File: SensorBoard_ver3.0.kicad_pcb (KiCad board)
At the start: 2 copper layers, 75 x 50 mm, 58 parts, among them IC1 MIC5504-3.3YM5-T5, J1 STLink, J10 Abs1, J11 Abs3, J12 Limit1, J13 Limit2, J14 Abs3, J2 Enc0, J3 Enc2, J4 CANConn, J5 Enc1, J6 Enc3, J7 CANConn, J8 Abs0, J9 Abs2, SW1 CAN_Terminal, SW2 IDSetSW, SW3 Reset, SW4 IDSetSW, U1 L7805, U2 MAX3485, U3 ATA6561, U4 STM32F303K8Tx, Y1 Crystal

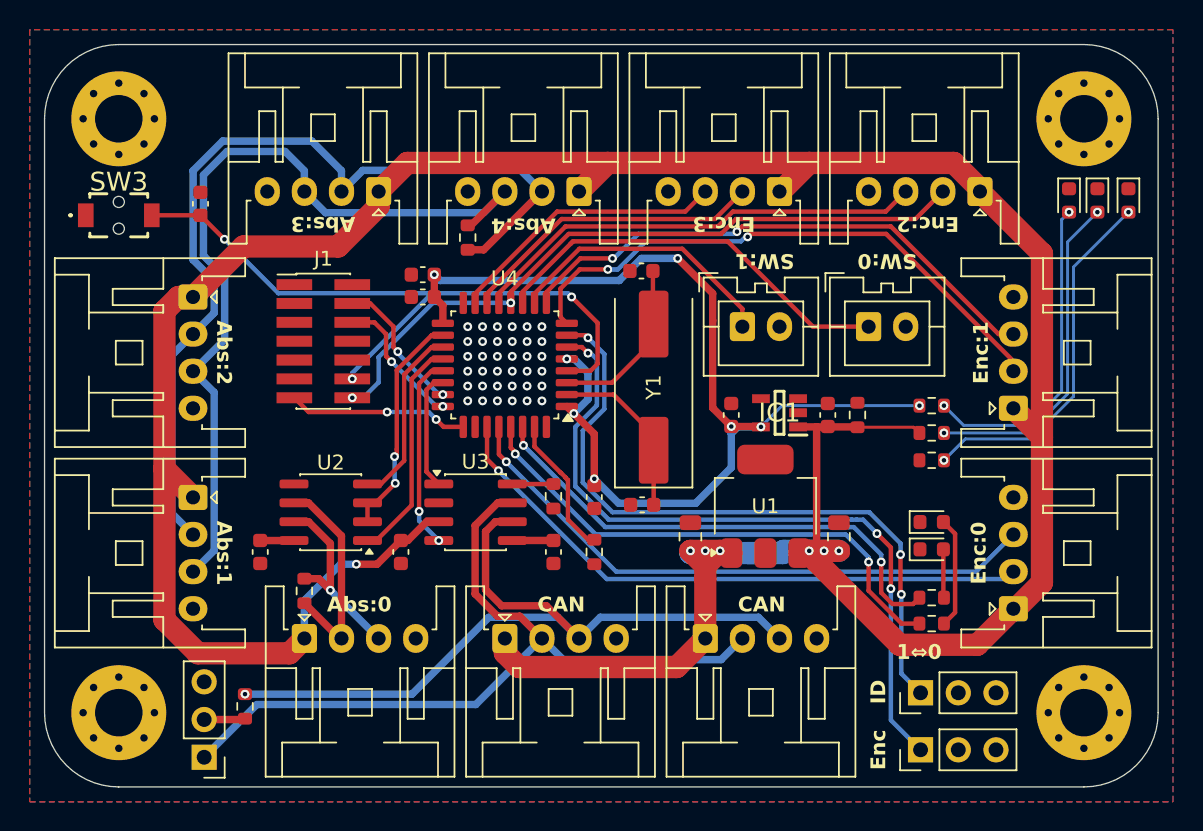
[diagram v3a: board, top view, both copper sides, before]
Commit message: ほとんど完成
残りすること
・終端抵抗の配線
・基板の見直し
・シルクの大型化
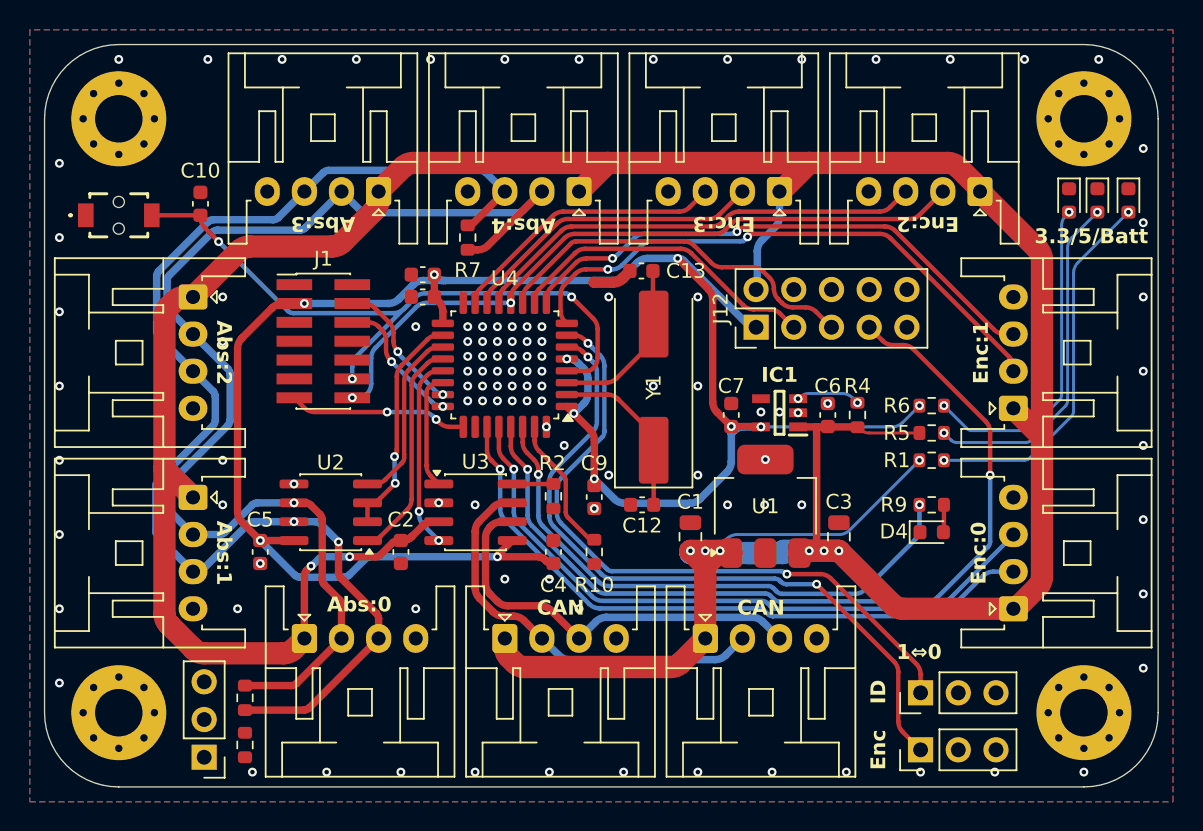
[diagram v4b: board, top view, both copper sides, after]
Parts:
- removed D5: LED, LED_SMD:LED_0603_1608Metric
- removed J13: Limit2, Connector_JST:JST_XA_B02B-XASK-1_1x02_P2.50mm_Vertical
- removed R11: 10kΩ, Resistor_SMD:R_0603_1608Metric
- J12: value Limit1 -> AddConn; footprint Connector_JST:JST_XA_B02B-XASK-1_1x02_P2.50mm_Vertical -> Connector_PinHeader_2.54mm:PinHeader_2x05_P2.54mm_Vertical
- moved R3 8.24 mm to (73.5, 84.0), turned to 90 degrees
- moved R9 6.25 mm to (119.8, 71.0)
- moved R8 2.60 mm to (73.5, 87.2), turned to -90 degrees
- moved D4 1.16 mm to (119.8, 72.8)
- moved J12 0.92 mm to (107.9, 59.0), turned to 90 degrees
- turned C4 to 90 degrees
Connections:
- J12 pad 1: /Add_PA4 -> +3.3V
- J12 pad 2: GND -> +5V
- SW3 pad 1: /NRST -> GND
- U4 pad 29: /LED2 -> /Add_PB6
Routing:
- net /Add_PB6: track 0.00 -> 60.3 mm, vias 0 -> 2
- net +3.3V: track 78.7 -> 134.8 mm, vias 8 -> 11
- net /LED2: track 35.2 -> 0.00 mm, vias 2 -> 0
- net /CANH: track 54.2 -> 27.8 mm
- net /CANL: track 53.6 -> 28.0 mm, vias 1 -> 0
- net VCC: track 31.2 -> 48.3 mm, vias 3 -> 4
- net /RS485_B: track 69.7 -> 84.8 mm, vias 1 -> 2
- net Net-(D5-A): track 7.48 -> 0.00 mm
- net /RS485_A: track 75.7 -> 83.0 mm, vias 0 -> 1
- net /EncB_0: track 40.8 -> 45.2 mm
- net Net-(IC1-EN): track 0.00 -> 4.31 mm, vias 0 -> 2
- net /LED1: track 34.0 -> 37.8 mm
- net /EncA_0: track 41.2 -> 44.6 mm
- net +5V: track 188.4 -> 191.7 mm, vias 4 -> 5
- net Net-(SW1-B): track 2.77 -> 0.00 mm
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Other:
- board text added: "3.3/5/Batt"
- board text removed: "SW:0"
- board text removed: "SW:1"

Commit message: ほとんど完成
再チェックして、発注したい
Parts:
- added R11: 10kΩ, Resistor_SMD:R_0603_1608Metric, B.Cu at (128.4, 75.2)
- added R12: 10kΩ, Resistor_SMD:R_0603_1608Metric, B.Cu at (128.4, 71.2)
- added R13: 10kΩ, Resistor_SMD:R_0603_1608Metric, B.Cu at (128.4, 77.2)
- added R14: 10kΩ, Resistor_SMD:R_0603_1608Metric, B.Cu at (128.4, 73.2)
- added R15: 10kΩ, Resistor_SMD:R_0603_1608Metric, B.Cu at (120.2, 46.7)
- added R16: 10kΩ, Resistor_SMD:R_0603_1608Metric, B.Cu at (122.2, 46.7)
- added R17: 10kΩ, Resistor_SMD:R_0603_1608Metric, B.Cu at (116.2, 46.7)
- added R18: 10kΩ, Resistor_SMD:R_0603_1608Metric, B.Cu at (118.2, 46.7)
- added R19: 10kΩ, Resistor_SMD:R_0603_1608Metric, B.Cu at (128.4, 61.8)
- added R20: 10kΩ, Resistor_SMD:R_0603_1608Metric, B.Cu at (128.4, 63.8)
- added R21: 10kΩ, Resistor_SMD:R_0603_1608Metric, B.Cu at (128.4, 57.8)
- added R22: 10kΩ, Resistor_SMD:R_0603_1608Metric, B.Cu at (128.4, 59.8)
- added R23: 10kΩ, Resistor_SMD:R_0603_1608Metric, B.Cu at (106.8, 46.7)
- added R24: 10kΩ, Resistor_SMD:R_0603_1608Metric, B.Cu at (108.8, 46.7)
- added R25: 10kΩ, Resistor_SMD:R_0603_1608Metric, B.Cu at (102.8, 46.7)
- added R26: 10kΩ, Resistor_SMD:R_0603_1608Metric, B.Cu at (104.8, 46.7)
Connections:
- J1 pad 14: /EncA_2 -> /EncA_1
- SW3 pad 1: GND -> /NRST
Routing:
- net /CANH: track 27.8 -> 51.4 mm, vias 0 -> 1
- net /EncA_1: track 39.0 -> 61.0 mm, vias 2 -> 4
- net /CANL: track 28.0 -> 50.0 mm, vias 0 -> 2
- net +5V: track 191.7 -> 209.2 mm, vias 5 -> 13
- net /EncA_2: track 47.0 -> 36.9 mm, vias 2 -> 0
- net Net-(D3-A): track 22.1 -> 17.0 mm
- net /EncB_3: track 18.8 -> 23.3 mm
- net /EncB_2: track 30.7 -> 35.1 mm
- net /EncA_3: track 20.5 -> 25.0 mm
- net /EncB_1: track 36.7 -> 41.1 mm
- net /EncB_0: track 45.2 -> 49.6 mm
- net /EncA_0: track 44.6 -> 49.1 mm
- net Net-(SW1-B): track 0.00 -> 3.09 mm
- net Net-(D2-A): track 23.3 -> 20.4 mm
- net Net-(D1-A): track 25.1 -> 24.0 mm
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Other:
- board text added: "+3.3V"
- board text added: "+5V"
- board text added: "<Desigin> Firmware : Jaga Hardware : Hama"
- board text added: "Sensor Board ver3.0"
- board text added: "↑Additional Conn GPIO:PB6/PA5/PA4"
- board text added: "↑CAN"
- board text added: "↓Caution! 12V⇔5V Select"
- board text added: "♨"
- board text added: "〈Size〉 ・50mm × 75mm ・40mm × 65mm"

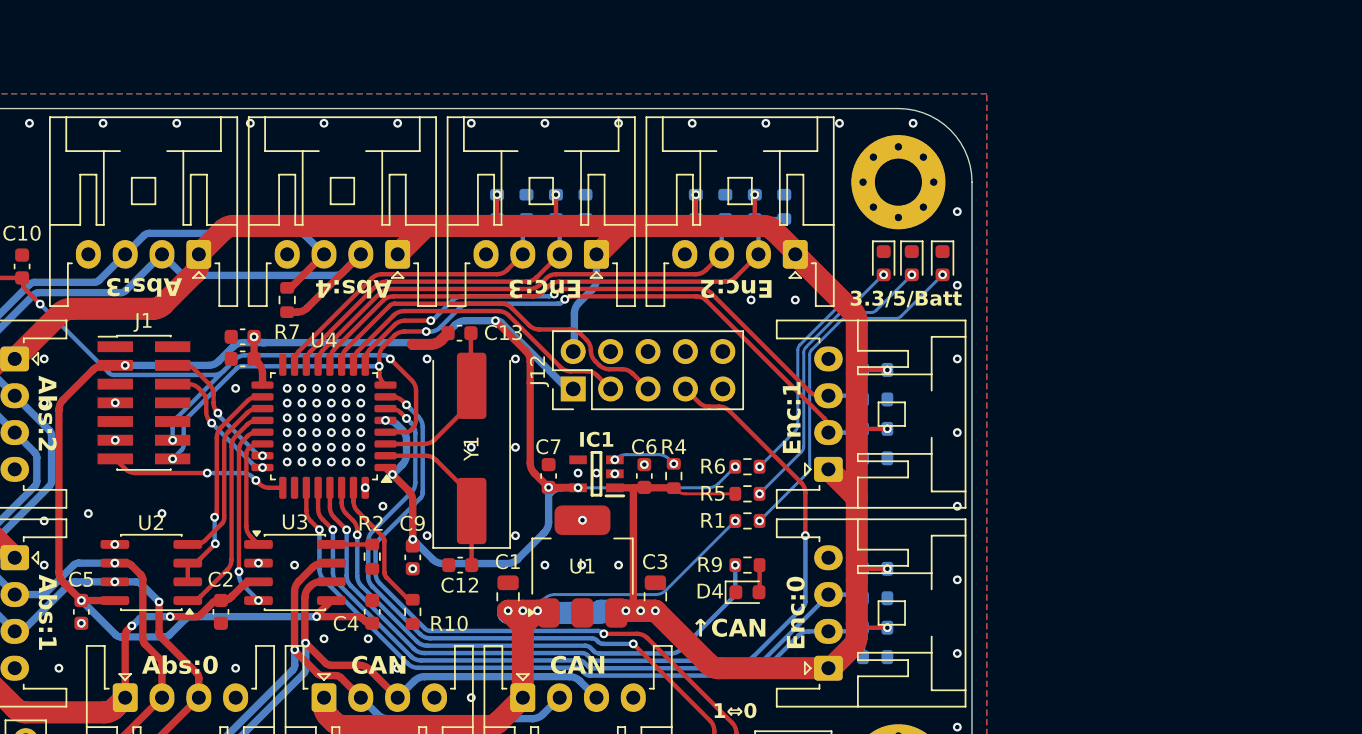
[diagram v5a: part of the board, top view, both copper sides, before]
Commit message: いろいろ修正
・フェライトビーズの追加
・シルクの追加
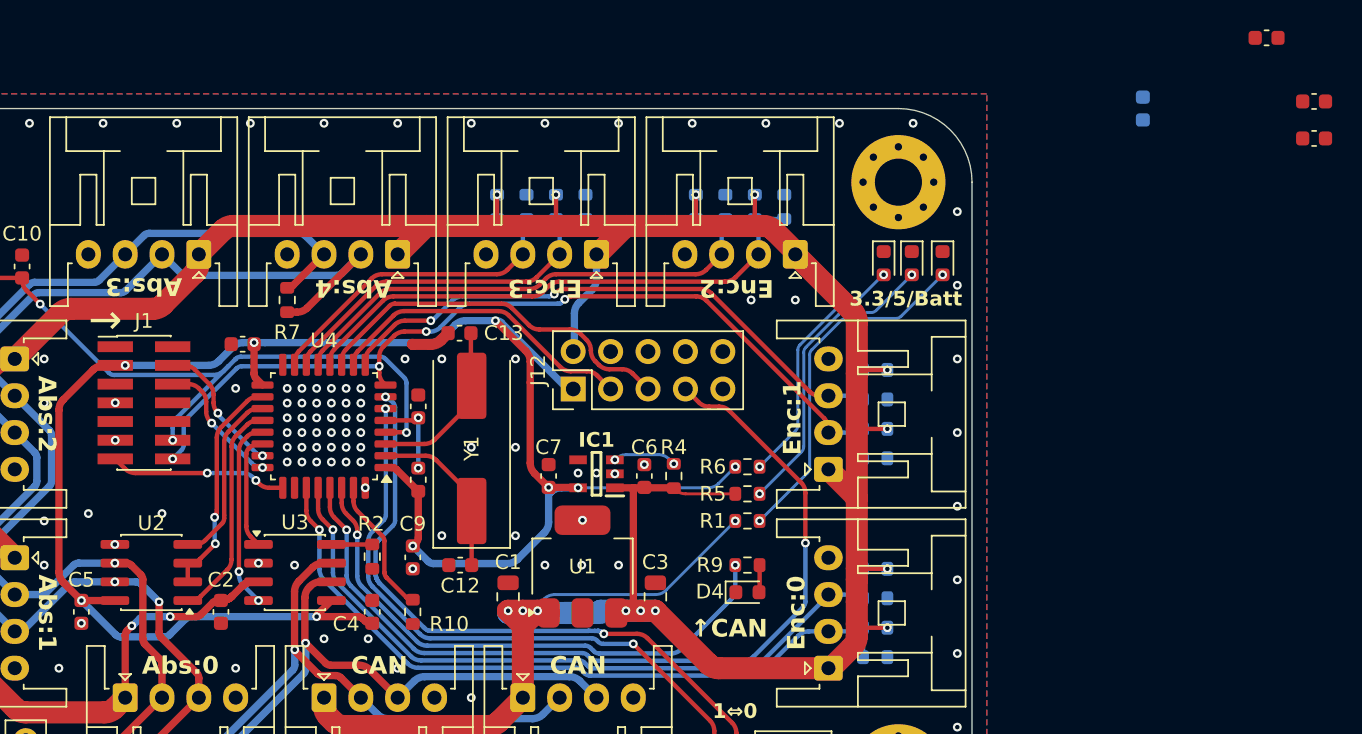
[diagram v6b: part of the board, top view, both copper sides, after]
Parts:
- added C14: 0.1μF, Capacitor_SMD:C_0603_1608Metric, B.Cu at (146.6, 40.0)
- added C15: 0.1μF, Capacitor_SMD:C_0603_1608Metric, F.Cu at (155.0, 35.2)
- added C16: 0.1μF, Capacitor_SMD:C_0603_1608Metric, F.Cu at (158.2, 39.5)
- added C17: 0.1μF, Capacitor_SMD:C_0603_1608Metric, F.Cu at (158.2, 42.0)
- added FB1: FB, Inductor_SMD:L_0603_1608Metric, F.Cu at (97.4, 65.2)
- added H5: Mark, SensorBoard_ver3.0:α-LumiCode, B.Cu at (77.1, 65.5)
- C11: value 1μF -> 0.1μF
- moved C8 12.8 mm to (97.4, 60.2), turned to 90 degrees
- moved C11 1.00 mm to (85.5, 56.0)
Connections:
- C8 pad 1: +3.3V -> +3.3VA
- U4 pad 5: +3.3V -> +3.3VA
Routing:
- net +3.3VA: track 0.00 -> 5.69 mm, vias 0 -> 2
- net +3.3V: track 134.8 -> 129.4 mm, vias 11 -> 9
- net /EncSW: track 47.8 -> 45.8 mm
- net /IDSet: track 45.2 -> 43.4 mm
- net /NRST: track 45.7 -> 44.9 mm
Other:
- board text added: "→"

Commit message: たぶんできた
たぶんできた
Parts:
- added C18: 0.1μF, Capacitor_SMD:C_0603_1608Metric, B.Cu at (75.2, 80.2)
- added C19: 0.1μF, Capacitor_SMD:C_0603_1608Metric, B.Cu at (67.2, 78.0)
- added C20: 0.1μF, Capacitor_SMD:C_0603_1608Metric, B.Cu at (67.2, 64.6)
- added C21: 0.1μF, Capacitor_SMD:C_0603_1608Metric, B.Cu at (80.2, 53.6)
- added C22: 0.1μF, Capacitor_SMD:C_0603_1608Metric, B.Cu at (97.8, 47.1)
- C15, C16, C17: moved to B.Cu
- moved C17 57.7 mm to (100.8, 46.7), turned to 90 degrees
- moved C16 44.6 mm to (114.2, 46.7), turned to 90 degrees
- moved C14 34.4 mm to (128.4, 69.2), turned to 0 degrees
- moved C15 33.6 mm to (128.4, 55.8)
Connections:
- SW3 pad 1: /NRST -> GND
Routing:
- net +5V: track 209.2 -> 211.2 mm, vias 13 -> 22
- net GND: vias 116 -> 119
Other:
- board text added: "C/U/D/U/D"

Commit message: 最終稿・発注した
発注したバージョン
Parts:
- moved C19 2.71 mm to (67.0, 75.3), turned to 90 degrees
- moved C20 2.66 mm to (67.0, 62.0), turned to 90 degrees
- moved C18 1.08 mm to (74.8, 79.2)
- moved C22 0.35 mm to (97.8, 46.8), turned to -90 degrees
- moved JP1 0.15 mm to (108.5, 74.1)
- moved C16 0.10 mm to (114.2, 46.8), turned to -90 degrees
- moved C17 0.10 mm to (100.8, 46.8), turned to -90 degrees
- moved R15 0.10 mm to (120.2, 46.8)
- moved R16 0.10 mm to (122.2, 46.8)
- moved R17 0.10 mm to (116.2, 46.8)
- moved R18 0.10 mm to (118.2, 46.8)
- moved R23 0.10 mm to (106.8, 46.8)
- moved R24 0.10 mm to (108.8, 46.8)
- moved R25 0.10 mm to (102.8, 46.8)
- moved R26 0.10 mm to (104.8, 46.8)
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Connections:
- J12 pad 4: GND -> /Add_PA4
- J12 pad 6: GND -> /Add_PA5
- J12 pad 8: GND -> /Add_PB6
- SW3 pad 1: GND -> /NRST
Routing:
- net +3.3V: track 129.4 -> 125.0 mm, vias 9 -> 8
- net /Add_PB6: track 60.3 -> 62.8 mm
- net /EncA_1: track 61.0 -> 59.1 mm
- net /Add_PA4: track 21.3 -> 22.9 mm
- net /Add_PA5: track 25.4 -> 26.7 mm
- net GND: track 2.71 -> 3.63 mm, vias 119 -> 127
- net +5V: track 211.2 -> 210.6 mm
- net /EncB_0: track 49.6 -> 49.0 mm
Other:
- board text added: "G N D"
